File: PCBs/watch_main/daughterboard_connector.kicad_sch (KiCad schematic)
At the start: 0 parts

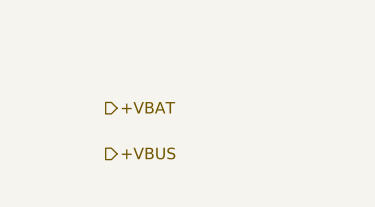
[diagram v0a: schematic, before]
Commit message: Created firmware project
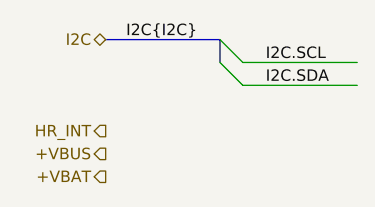
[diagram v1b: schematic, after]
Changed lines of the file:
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@@
 (kicad_sch (version 20230121) (generator eeschema)
   (paper "A4")
-  (hierarchical_label "+VBAT" (shape output) (at 66.04 86.36 0) (fields_autoplaced)
-    (effects (font (size 1.27 1.27)) (justify left))
+  (bus_entry (at 78.74 81.28) (size 2.54 2.54)
+    (stroke (width 0) (type default))
   )
-  (hierarchical_label "+VBUS" (shape output) (at 66.04 91.44 0) (fields_autoplaced)
-    (effects (font (size 1.27 1.27)) (justify left))
+  (bus_entry (at 78.74 78.74) (size 2.54 2.54)
+    (stroke (width 0) (type default))
+  )
+  (bus (pts (xy 78.74 78.74) (xy 66.04 78.74))
+    (stroke (width 0) (type default))
+  )
+  (bus (pts (xy 78.74 78.74) (xy 78.74 81.28))
+    (stroke (width 0) (type default))
+  )
+  (wire (pts (xy 81.28 81.28) (xy 93.98 81.28))
+    (stroke (width 0) (type default))
+  )
+  (wire (pts (xy 81.28 83.82) (xy 93.98 83.82))
+    (stroke (width 0) (type default))
+  )
+  (label "I2C.SDA" (at 83.82 83.82 0) (fields_autoplaced)
+    (effects (font (size 1.27 1.27)) (justify left bottom))
+  )
+  (label "I2C{I2C}" (at 76.2 78.74 180) (fields_autoplaced)
+    (effects (font (size 1.27 1.27)) (justify right bottom))
+  )
+  (label "I2C.SCL" (at 83.82 81.28 0) (fields_autoplaced)
+    (effects (font (size 1.27 1.27)) (justify left bottom))
+  )
+  (hierarchical_label "HR_INT" (shape output) (at 66.04 88.9 180) (fields_autoplaced)
+    (effects (font (size 1.27 1.27)) (justify right))
+  )
+  (hierarchical_label "+VBAT" (shape output) (at 66.04 93.98 180) (fields_autoplaced)
+    (effects (font (size 1.27 1.27)) (justify right))
+  )
+  (hierarchical_label "I2C" (shape bidirectional) (at 66.04 78.74 180) (fields_autoplaced)
+    (effects (font (size 1.27 1.27)) (justify right))
+    (property "DSI" "DSI" (at 66.04 80.01 0)
+      (effects (font (size 1.27 1.27) italic) (justify right) hide)
+    )
+  )
+  (hierarchical_label "+VBUS" (shape output) (at 66.04 91.44 180) (fields_autoplaced)
+    (effects (font (size 1.27 1.27)) (justify right))
   )
 )

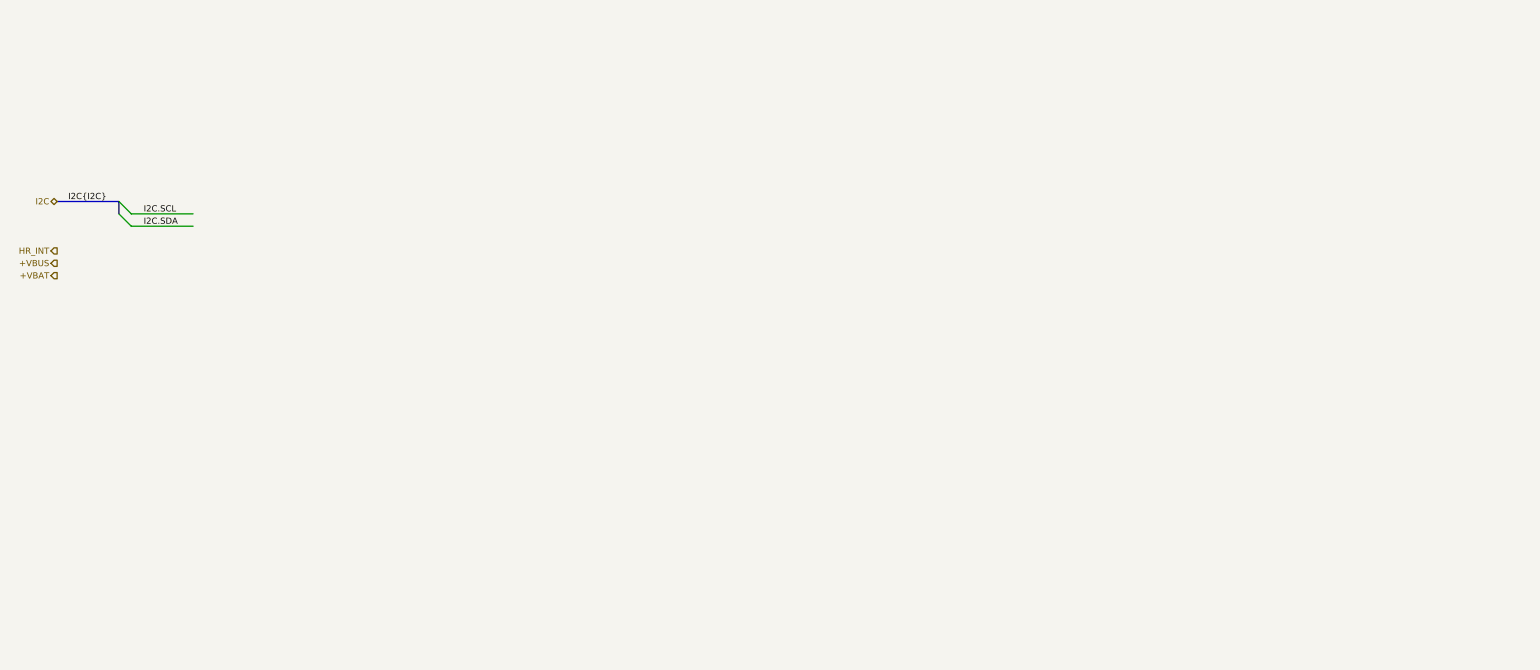
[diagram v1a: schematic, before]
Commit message: Added connector symbols and footprints
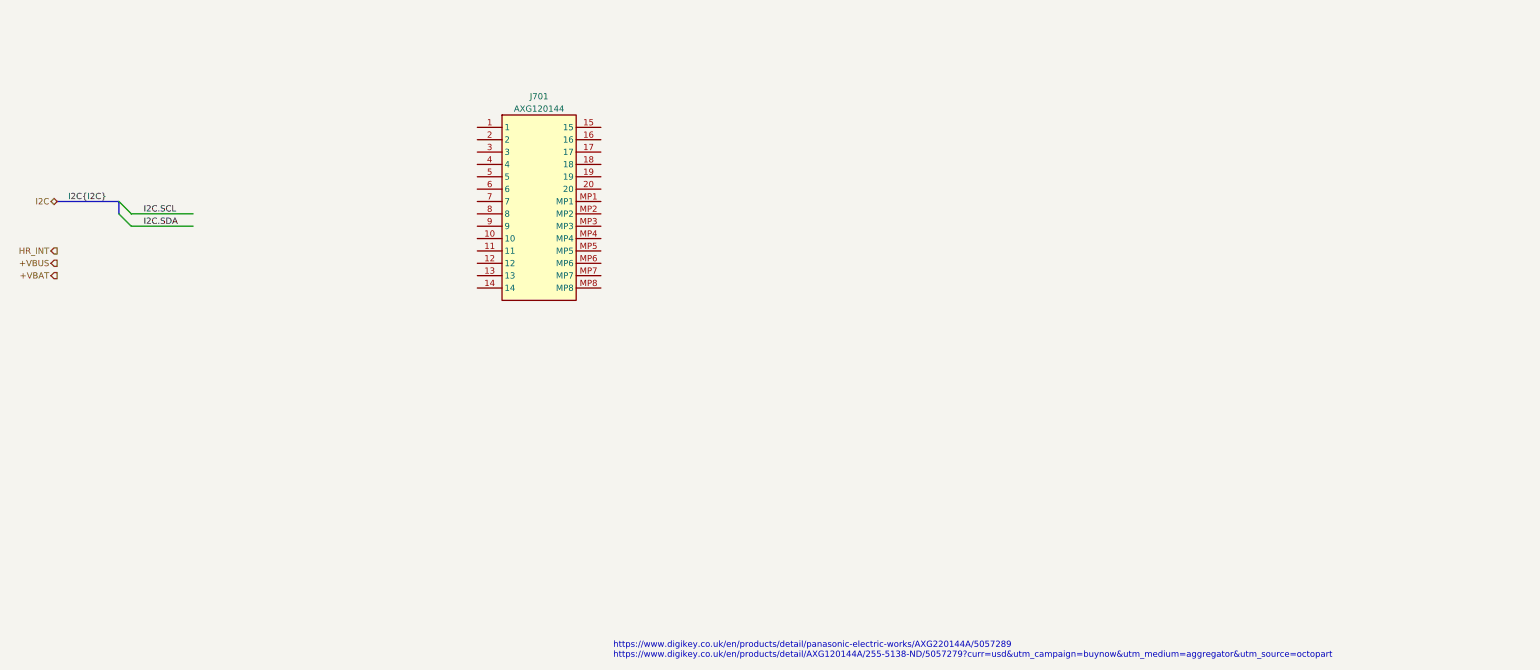
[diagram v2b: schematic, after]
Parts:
- added J701: AXG120144, AXG120144, symbol AXG120144:AXG120144
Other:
- note added: "https://www.digikey.co.uk/en/products/detail/panasonic-electric-works/AXG220144A/5057289 https://www.digikey.co.uk/en/products/detail/AXG120144A/255-5138-ND/5057279?curr=usd&utm_campaign=buynow&utm_medium=aggregator&utm_source=octopart"
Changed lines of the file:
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@@
     (stroke (width 0) (type default))
+  )
+  (text "https://www.digikey.co.uk/en/products/detail/panasonic-electric-works/AXG220144A/5057289\nhttps://www.digikey.co.uk/en/products/detail/AXG120144A/255-5138-ND/5057279?curr=usd&utm_campaign=buynow&utm_medium=aggregator&utm_source=octopart"
+    (at 180.34 172.72 0)
+    (effects (font (size 1.27 1.27)) (justify left bottom))
   )
   (label "I2C.SDA" (at 83.82 83.82 0) (fields_autoplaced)
@@
     (effects (font (size 1.27 1.27)) (justify right))
   )
+  (symbol (lib_id "AXG120144:AXG120144") (at 152.4 63.5 0) (unit 1)
+    (in_bom yes) (on_board yes) (dnp no) (fields_autoplaced)
+    (property "Reference" "J701" (at 165.1 57.15 0)
+      (effects (font (size 1.27 1.27)))
+    )
+    (property "Value" "AXG120144" (at 165.1 59.69 0)
+      (effects (font (size 1.27 1.27)))
+    )
+    (property "Footprint" "AXG120144" (at 173.99 158.42 0)
+      (effects (font (size 1.27 1.27)) (justify left top) hide)
+    )
+    (property "Datasheet" "https://www3.panasonic.biz/ac/e_download/control/connector/base-fpc/catalog/con_eng_s35.pdf?f_cd=401984&via=ok" (at 173.99 258.42 0)
+      (effects (font (size 1.27 1.27)) (justify left top) hide)
+    )
+    (property "Height" "0.79" (at 173.99 458.42 0)
+      (effects (font (size 1.27 1.27)) (justify left top) hide)
+    )
+    (property "Manufacturer_Name" "Panasonic" (at 173.99 558.42 0)
+      (effects (font (size 1.27 1.27)) (justify left top) hide)
+    )
+    (property "Manufacturer_Part_Number" "AXG120144" (at 173.99 658.42 0)
+      (effects (font (size 1.27 1.27)) (justify left top) hide)
+    )
+    (property "Mouser Part Number" "769-AXG120144" (at 173.99 758.42 0)
+      (effects (font (size 1.27 1.27)) (justify left top) hide)
+    )
+    (property "Mouser Price/Stock" "https://www.mouser.co.uk/ProductDetail/Panasonic-Industrial-Devices/AXG120144?qs=MNIFWdyJgbqXw6rsxlm2Ww%3D%3D" (at 173.99 858.42 0)
+      (effects (font (size 1.27 1.27)) (justify left top) hide)
+    )
+    (property "Arrow Part Number" "AXG120144" (at 173.99 958.42 0)
+      (effects (font (size 1.27 1.27)) (justify left top) hide)
+    )
+    (property "Arrow Price/Stock" "https://www.arrow.com/en/products/axg120144/panasonic?region=nac" (at 173.99 1058.42 0)
+      (effects (font (size 1.27 1.27)) (justify left top) hide)
+    )
+    (pin "1")
+    (pin "10")
+    (pin "11")
+    (pin "12")
+    (pin "13")
+    (pin "14")
+    (pin "15")
+    (pin "16")
+    (pin "17")
+    (pin "18")
+    (pin "19")
+    (pin "2")
+    (pin "20")
+    (pin "3")
+    (pin "4")
+    (pin "5")
+    (pin "6")
+    (pin "7")
+    (pin "8")
+    (pin "9")
+    (pin "MP1")
+    (pin "MP2")
+    (pin "MP3")
+    (pin "MP4")
+    (pin "MP5")
+    (pin "MP6")
+    (pin "MP7")
+    (pin "MP8")
+    (instances
+      (project "watch_main"
+        (path "/b008648a-c7cf-4e14-8a0a-b9314d757b4a/b8b2906b-c578-47bc-a414-19d0aaf7d65f"
+          (reference "J701") (unit 1)
+        )
+      )
+    )
+  )
 )

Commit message: Main PCB schematic almost complete
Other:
- note added: "HR sensors address = 0x57"
- note added: "LRA driver address = 0x5A"
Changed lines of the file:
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@@
+    (effects (font (size 1.27 1.27)) (justify left bottom))
+  )
+  (text "HR sensors address = 0x57" (at 109.22 132.08 0)
+    (effects (font (size 1.27 1.27)) (justify left bottom))
+  )
+  (text "LRA driver address = 0x5A" (at 109.22 134.62 0)
     (effects (font (size 1.27 1.27)) (justify left bottom))
   )

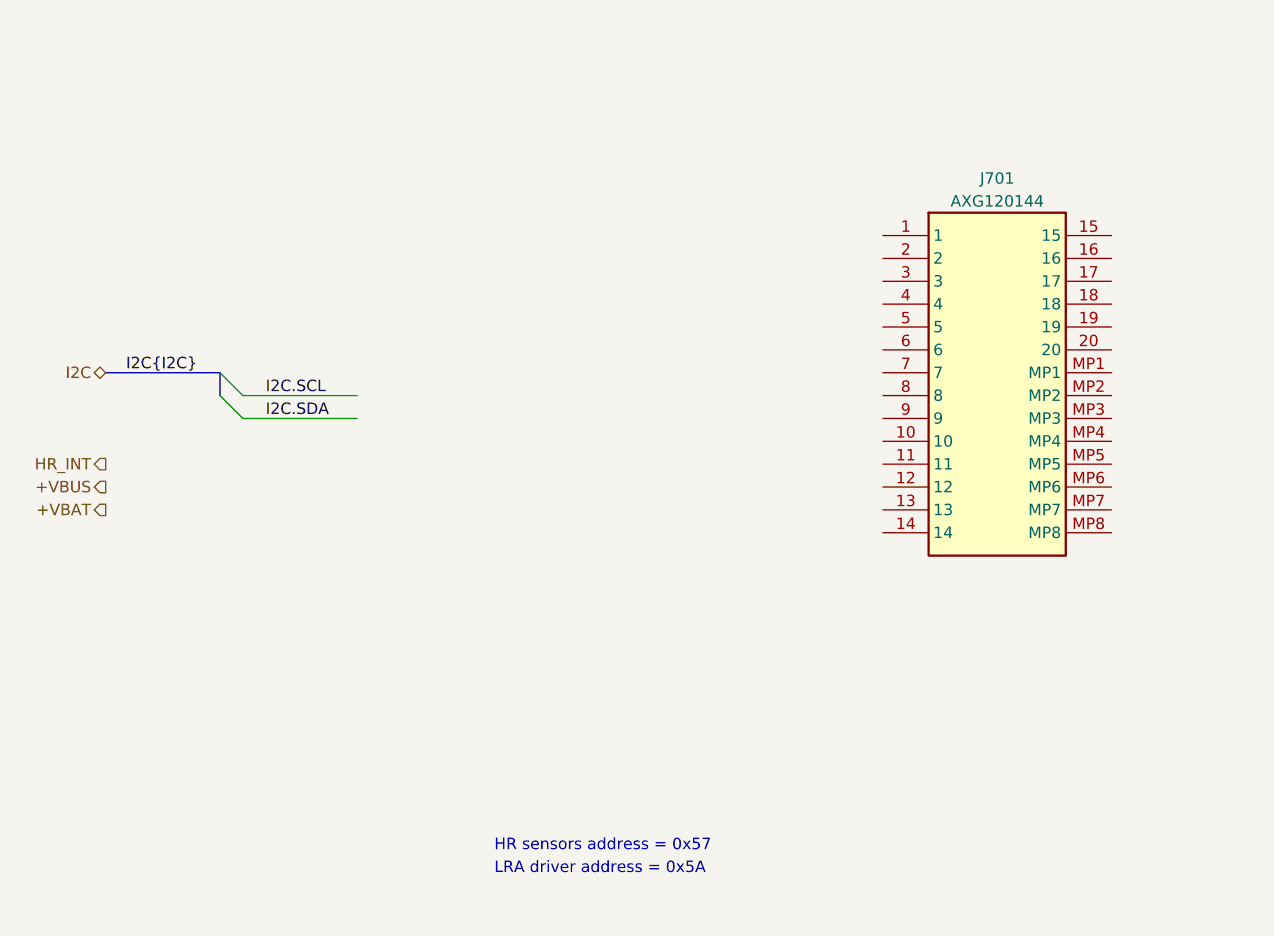
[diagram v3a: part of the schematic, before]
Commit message: Progress with schematic and RFID simulations
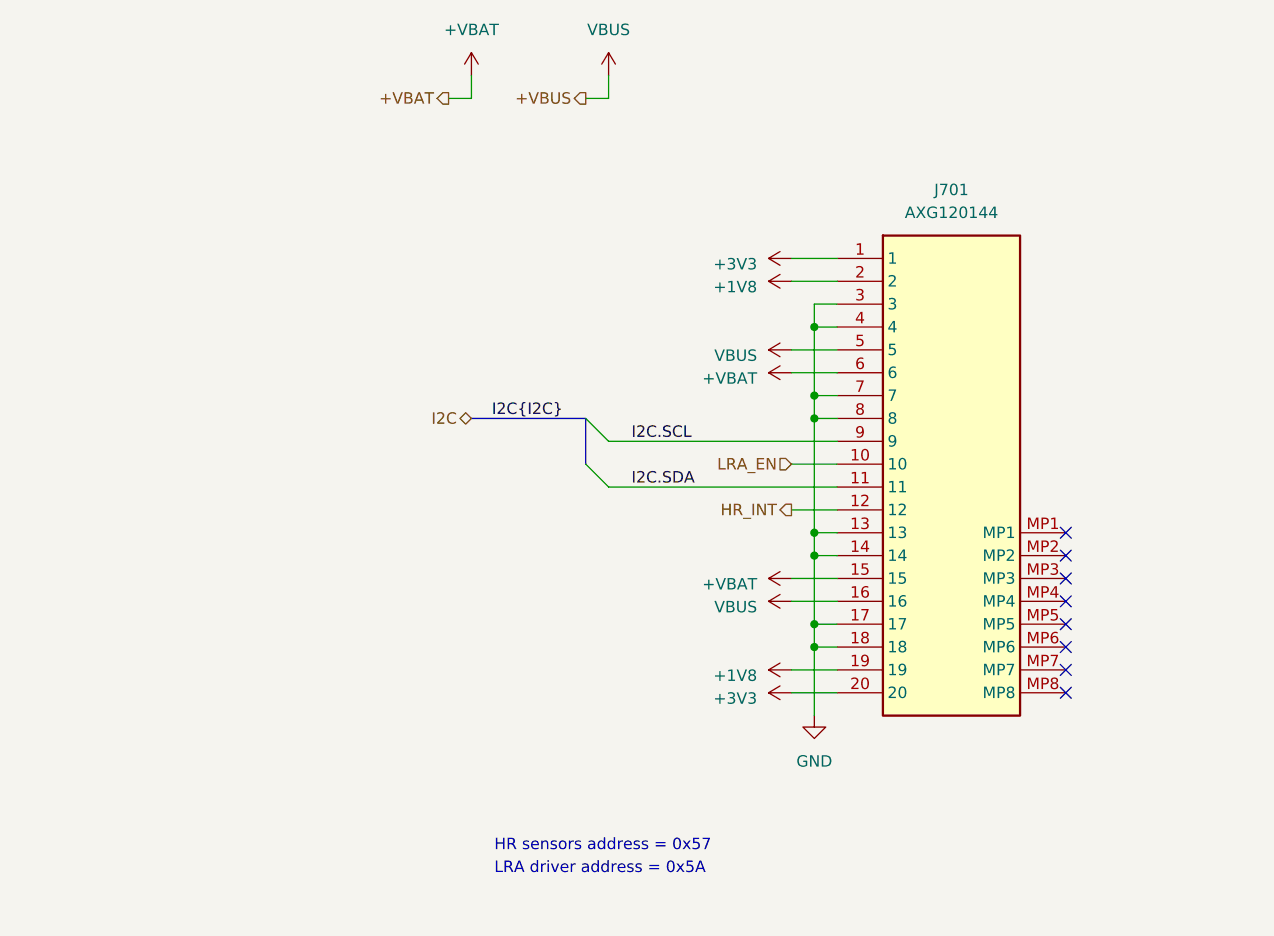
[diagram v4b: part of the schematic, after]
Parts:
- J701: footprint AXG120144 -> watch_footprints:AXG120144
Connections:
- net +VBAT: now also J701.15, J701.6
- net HR_INT: now also J701.12
- net I2C.SCL: now also J701.9
- net I2C.SDA: now also J701.11
- net +3V3: now reaches J701.1
- net +3V3: now also J701.20
- net LRA_EN: now reaches J701.10
- net GND: now reaches J701.13
- net GND: now also J701.14, J701.17, J701.18, J701.3, J701.4, J701.7, J701.8
- net VBUS: now reaches J701.16
- net VBUS: now also J701.5
- net +1V8: now reaches J701.19
- net +1V8: now also J701.2
- no-connect marks 0 -> 8
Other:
- moved on the sheet: J701

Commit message: Started routing main PCB
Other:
- note removed: "https://www.digikey.co.uk/en/products/detail/panasonic-electric-works/AXG220144A/5057289 https://www.digikey.co.uk/en/products/detail/AXG120144A/255-5138-ND/5057279?curr=usd&utm_campaign=buynow&utm_medium=aggregator&utm_source=octopart"
- title: (none) -> Watch Daughterboard Connector
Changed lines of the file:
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@@
   (paper "A4")
   (title_block
+    (title "Watch Daughterboard Connector")
+    (date "2023-12-21")
     (rev "1")
+    (comment 1 "Checked by Ben Smith 21/12/23")
   )
   (junction (at 144.78 99.06) (diameter 0) (color 0 0 0 0)
@@
     (stroke (width 0) (type default))
   )
-  (text "https://www.digikey.co.uk/en/products/detail/panasonic-electric-works/AXG220144A/5057289\nhttps://www.digikey.co.uk/en/products/detail/AXG120144A/255-5138-ND/5057279?curr=usd&utm_campaign=buynow&utm_medium=aggregator&utm_source=octopart"
-    (at 180.34 172.72 0)
-    (effects (font (size 1.27 1.27)) (justify left bottom))
-  )
   (text "HR sensors address = 0x57" (at 109.22 132.08 0)
     (effects (font (size 1.27 1.27)) (justify left bottom))
@@
   (symbol (lib_id "power:+1V8") (at 142.24 68.58 90) (unit 1)
     (in_bom yes) (on_board yes) (dnp no) (fields_autoplaced)
-    (property "Reference" "#PWR0705" (at 146.05 68.58 0)
+    (property "Reference" "#PWR0704" (at 146.05 68.58 0)
       (effects (font (size 1.27 1.27)) hide)
     )
@@
       (project "watch_main"
         (path "/b008648a-c7cf-4e14-8a0a-b9314d757b4a/b8b2906b-c578-47bc-a414-19d0aaf7d65f"
-          (reference "#PWR0705") (unit 1)
+          (reference "#PWR0704") (unit 1)
         )
       )
@@
         )
         (path "/b008648a-c7cf-4e14-8a0a-b9314d757b4a/b8b2906b-c578-47bc-a414-19d0aaf7d65f"
-          (reference "#PWR0709") (unit 1)
+          (reference "#PWR0701") (unit 1)
         )
       )
@@
         )
         (path "/b008648a-c7cf-4e14-8a0a-b9314d757b4a/b8b2906b-c578-47bc-a414-19d0aaf7d65f"
-          (reference "#PWR0702") (unit 1)
+          (reference "#PWR0706") (unit 1)
         )
       )
@@
   (symbol (lib_id "power:GND") (at 144.78 116.84 0) (unit 1)
     (in_bom yes) (on_board yes) (dnp no) (fields_autoplaced)
-    (property "Reference" "#PWR0701" (at 144.78 123.19 0)
+    (property "Reference" "#PWR0711" (at 144.78 123.19 0)
       (effects (font (size 1.27 1.27)) hide)
     )
@@
       (project "watch_main"
         (path "/b008648a-c7cf-4e14-8a0a-b9314d757b4a/b8b2906b-c578-47bc-a414-19d0aaf7d65f"
-          (reference "#PWR0701") (unit 1)
+          (reference "#PWR0711") (unit 1)
         )
       )
@@
         )
         (path "/b008648a-c7cf-4e14-8a0a-b9314d757b4a/b8b2906b-c578-47bc-a414-19d0aaf7d65f"
-          (reference "#PWR0710") (unit 1)
+          (reference "#PWR0702") (unit 1)
         )
       )
@@
         )
         (path "/b008648a-c7cf-4e14-8a0a-b9314d757b4a/b8b2906b-c578-47bc-a414-19d0aaf7d65f"
-          (reference "#PWR0706") (unit 1)
+          (reference "#PWR0705") (unit 1)
         )
       )
@@
   (symbol (lib_id "power:+3V3") (at 142.24 114.3 90) (unit 1)
     (in_bom yes) (on_board yes) (dnp no) (fields_autoplaced)
-    (property "Reference" "#PWR0704" (at 146.05 114.3 0)
+    (property "Reference" "#PWR0710" (at 146.05 114.3 0)
       (effects (font (size 1.27 1.27)) hide)
     )
@@
       (project "watch_main"
         (path "/b008648a-c7cf-4e14-8a0a-b9314d757b4a/b8b2906b-c578-47bc-a414-19d0aaf7d65f"
-          (reference "#PWR0704") (unit 1)
+          (reference "#PWR0710") (unit 1)
         )
       )
@@
   (symbol (lib_id "power:+1V8") (at 142.24 111.76 90) (unit 1)
     (in_bom yes) (on_board yes) (dnp no) (fields_autoplaced)
-    (property "Reference" "#PWR0711" (at 146.05 111.76 0)
+    (property "Reference" "#PWR0709" (at 146.05 111.76 0)
       (effects (font (size 1.27 1.27)) hide)
     )
@@
       (project "watch_main"
         (path "/b008648a-c7cf-4e14-8a0a-b9314d757b4a/b8b2906b-c578-47bc-a414-19d0aaf7d65f"
-          (reference "#PWR0711") (unit 1)
+          (reference "#PWR0709") (unit 1)
         )
       )
@@
   (symbol (lib_id "power:+3V3") (at 142.24 66.04 90) (unit 1)
     (in_bom yes) (on_board yes) (dnp no) (fields_autoplaced)
-    (property "Reference" "#PWR0708" (at 146.05 66.04 0)
+    (property "Reference" "#PWR0703" (at 146.05 66.04 0)
       (effects (font (size 1.27 1.27)) hide)
     )
@@
       (project "watch_main"
         (path "/b008648a-c7cf-4e14-8a0a-b9314d757b4a/b8b2906b-c578-47bc-a414-19d0aaf7d65f"
-          (reference "#PWR0708") (unit 1)
+          (reference "#PWR0703") (unit 1)
         )
       )
@@
         )
         (path "/b008648a-c7cf-4e14-8a0a-b9314d757b4a/b8b2906b-c578-47bc-a414-19d0aaf7d65f"
-          (reference "#PWR0703") (unit 1)
-        )
-      )
+          (reference "#PWR0708") (unit 1)
+        )
+      )
